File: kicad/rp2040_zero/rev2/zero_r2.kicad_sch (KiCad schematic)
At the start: 14 parts, among them J1 jtag, J2 Conn_01x03_Socket, J3 Debug port, J5 Debug port, U1 RP2040-Zero, U3 3V->VTREF, U4 VTREF->3V, U5 VTREF<->3V, U6 RT9013-33GB

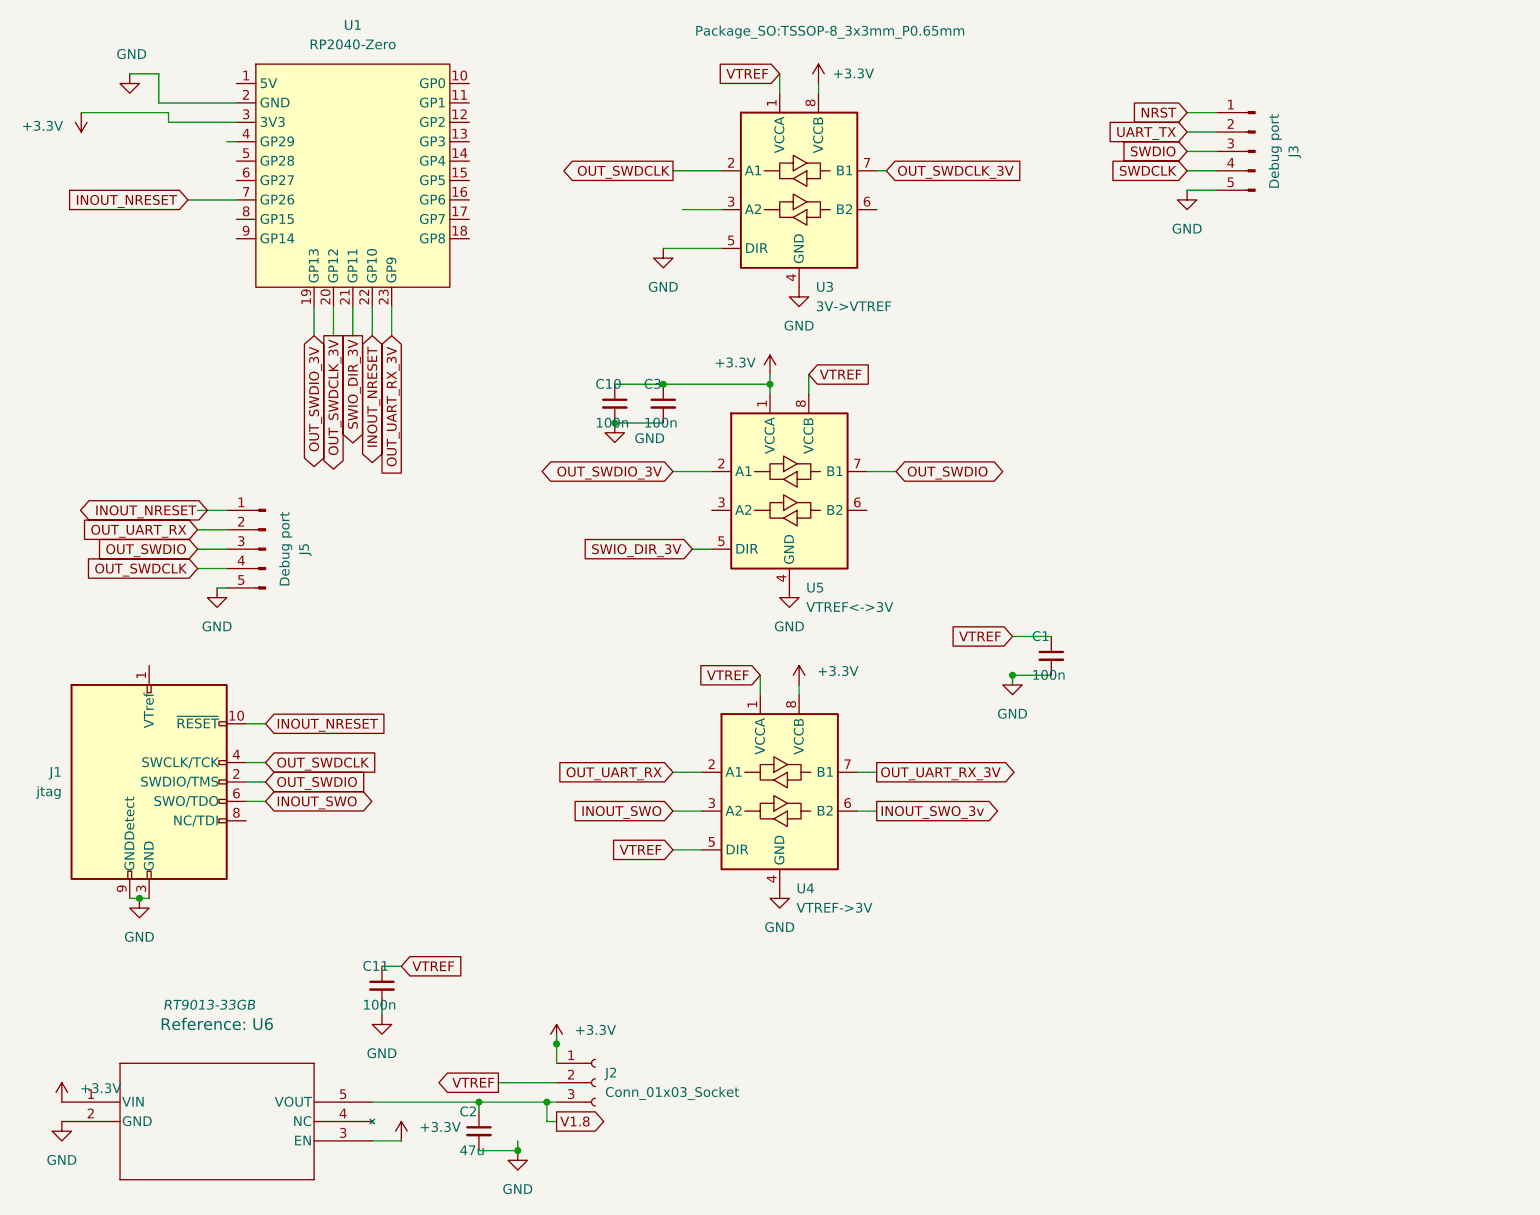
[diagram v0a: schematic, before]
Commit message: Kicad update: ch32: update pcb , add boot pin control ch32: Ground PB2 so that the internal bootloader is on USB rp_zero_mini :add mostfet to rp zero mini
general update
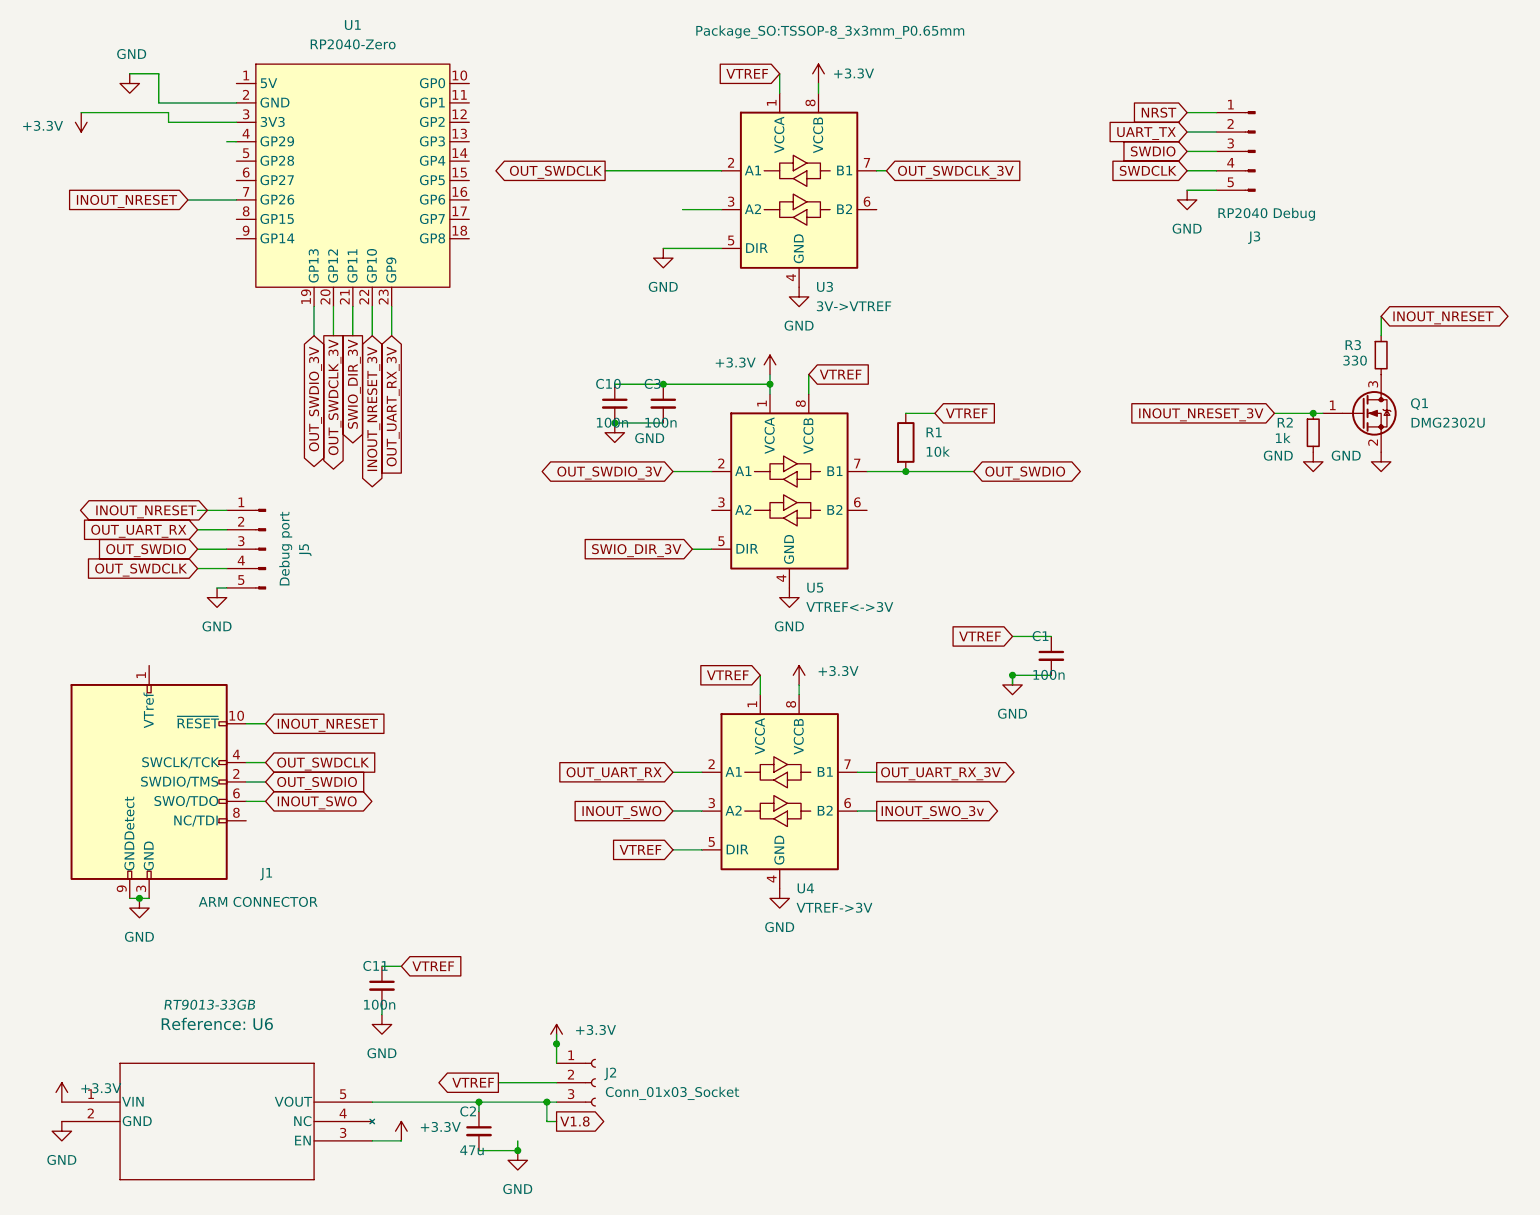
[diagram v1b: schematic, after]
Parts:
- added Q1: DMG2302U, Package_TO_SOT_SMD:SOT-23, symbol Transistor_FET:DMG2302U
- added R1: 10k, Resistor_SMD:R_0603_1608Metric, symbol Device:R
- added R2: 1k, Resistor_SMD:R_0603_1608Metric, symbol Device:R_Small
- added R3: 330, Resistor_SMD:R_0603_1608Metric, symbol Device:R_Small
- J1: value jtag -> ARM CONNECTOR
- J3: value Debug port -> RP2040 Debug
- J5: footprint Con5 -> Connector_JST:JST_XH_B5B-XH-A_1x05_P2.50mm_Vertical
- U6: footprint PCM_Package_TO_SOT_SMD_AKL:TSOT-23-5 -> Package_TO_SOT_SMD:SOT-23-5_HandSoldering
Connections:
- net GND: now also Q1.2 (S), R2.2
- net INOUT_NRESET: now also R3.1; no longer U1.22 (GP10)
- net OUT_SWDIO: now also R1.2
- net VTREF: now also R1.1
- new net: Q1.3 (D), R3.2
- new net INOUT_NRESET_3V: Q1.1 (G), R2.1, U1.22 (GP10)
